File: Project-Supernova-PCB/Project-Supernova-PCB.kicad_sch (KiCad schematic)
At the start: 65 parts, among them J1 Conn_01x04, J10 Conn_01x02, J11 Screw_Terminal_01x02, J12 Screw_Terminal_01x02, J13 Conn_01x04, J14 Conn_01x04, J15 Conn_01x04, J2 Conn_01x04, J3 Conn_01x04, J4 Conn_Coaxial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

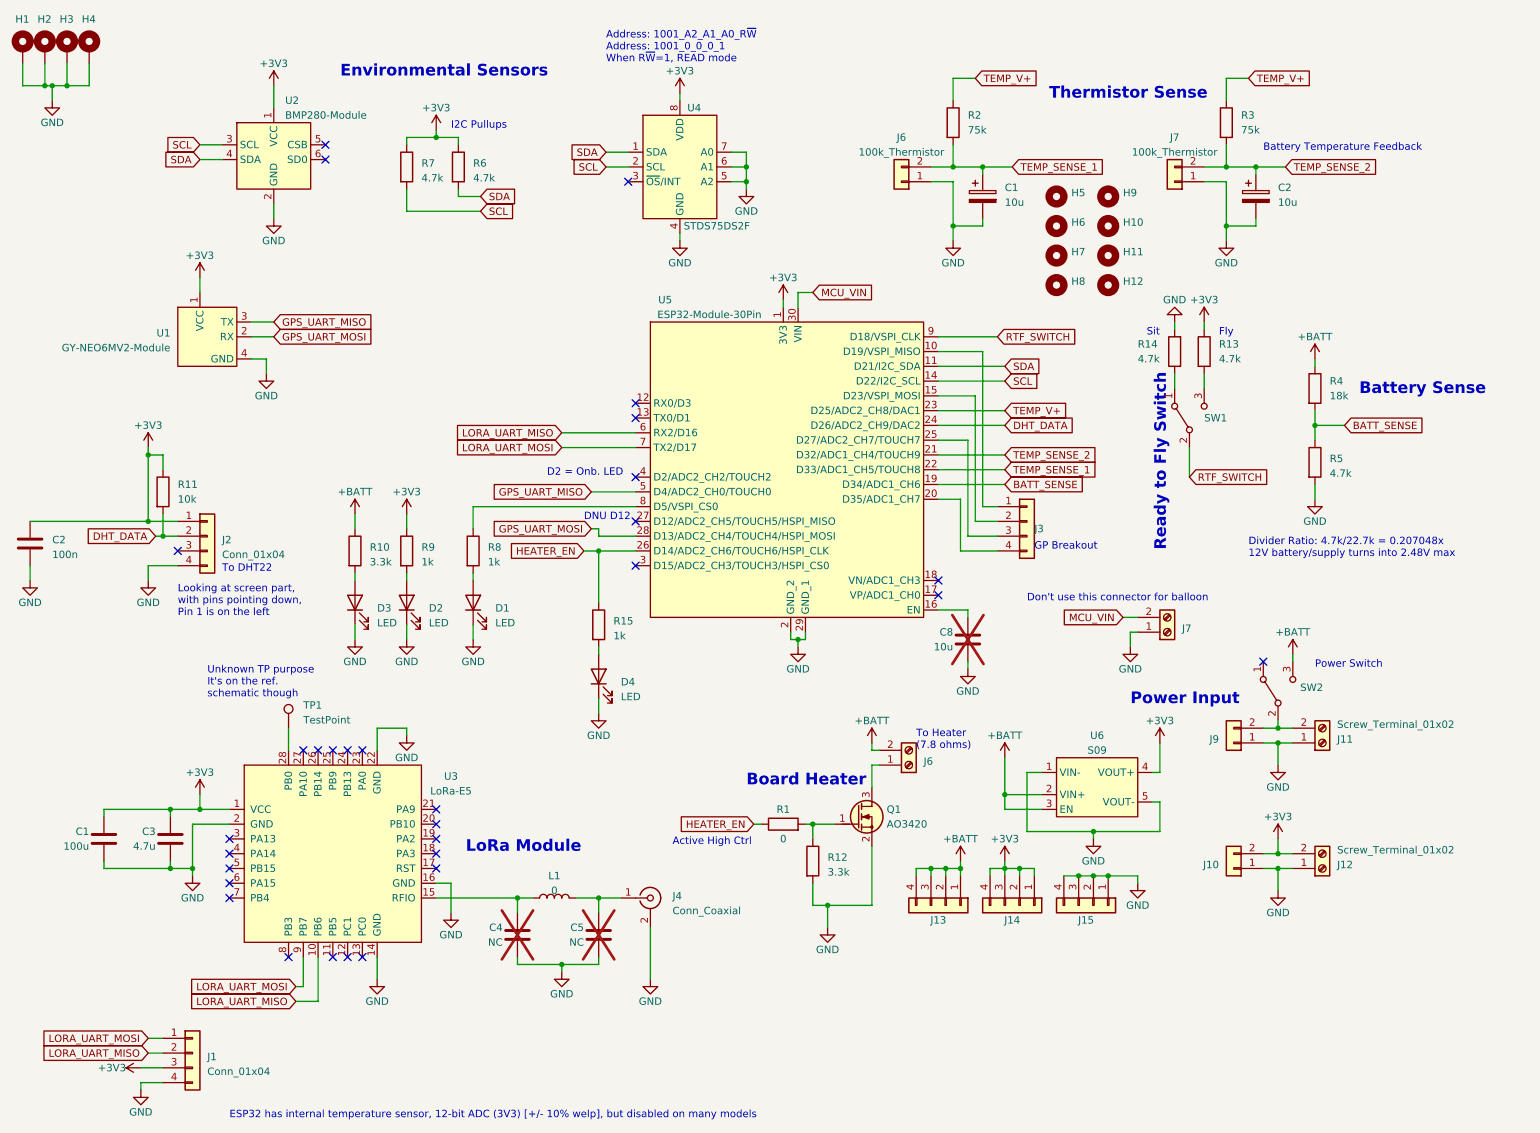
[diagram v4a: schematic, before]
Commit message: Clean up very messy schematic
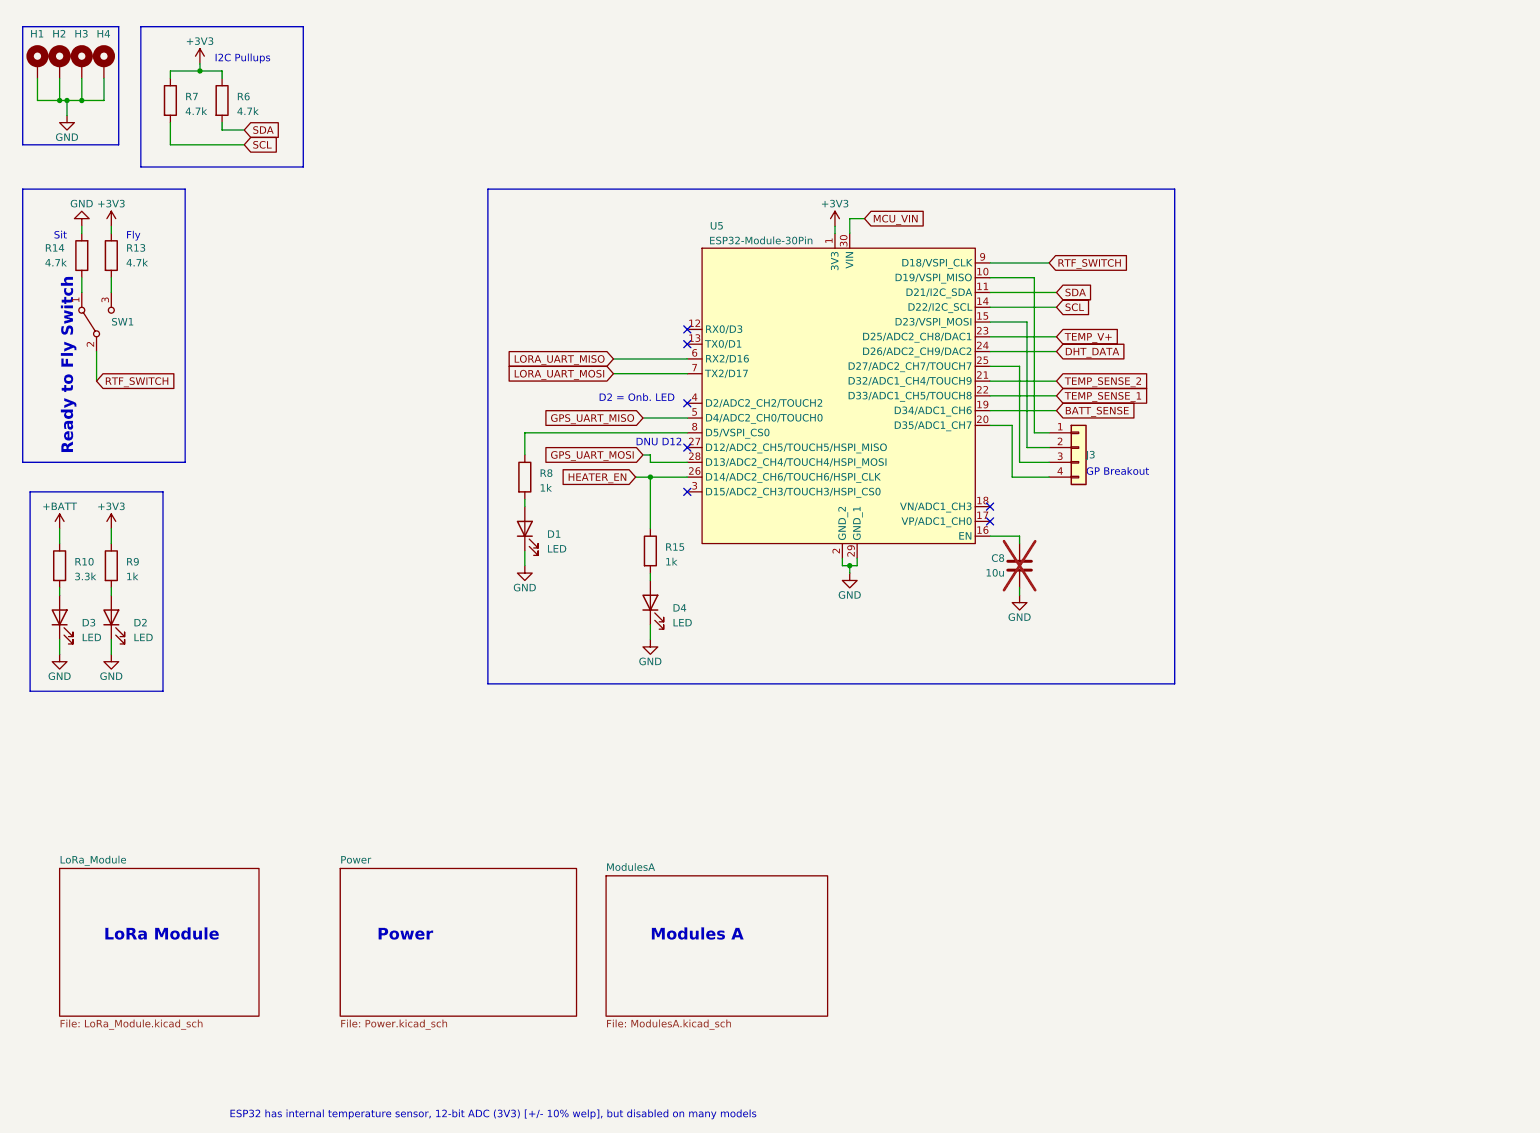
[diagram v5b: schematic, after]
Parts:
- removed C1, C2: 10u, Capacitor_SMD:C_1206_3216Metric_Pad1.33x1.80mm_HandSolder, symbol Device:C_Polarized
- removed C1: 100u, Capacitor_SMD:C_1206_3216Metric_Pad1.33x1.80mm_HandSolder, symbol Device:C
- removed C2: 100n, Capacitor_SMD:C_1206_3216Metric_Pad1.33x1.80mm_HandSolder, symbol Device:C
- removed C3: 4.7u, Capacitor_SMD:C_1206_3216Metric_Pad1.33x1.80mm_HandSolder, symbol Device:C
- removed C4, C5: NC, Capacitor_SMD:C_1206_3216Metric_Pad1.33x1.80mm_HandSolder, symbol Device:C
- removed H10, H11, H12, H5, H6, H7, H8, H9: MountingHole, MountingHole:MountingHole_2mm, symbol Mechanical:MountingHole
- removed J1, J13, J14, J15, J2: Conn_01x04, Connector_PinHeader_2.54mm:PinHeader_1x04_P2.54mm_Vertical, symbol Connector_Generic:Conn_01x04
- removed J10, J9: Conn_01x02, Connector_PinHeader_2.54mm:PinHeader_1x02_P2.54mm_Vertical, symbol Connector_Generic:Conn_01x02
- removed J11, J12, J6, J7: Screw_Terminal_01x02, TerminalBlock:TerminalBlock_bornier-2_P5.08mm, symbol Connector:Screw_Terminal_01x02
- removed J4: Conn_Coaxial, Connector_Coaxial:SMA_Wurth_60312002114503_Vertical, symbol Connector:Conn_Coaxial
- removed J6, J7: 100k_Thermistor, Connector_PinHeader_2.54mm:PinHeader_1x02_P2.54mm_Vertical, symbol Connector_Generic:Conn_01x02
- removed L1: 0, Inductor_SMD:L_1206_3216Metric_Pad1.42x1.75mm_HandSolder, symbol Device:L
- removed Q1: AO3420, Project-Supernova-Footprint-Lib:SOT-23-MassivePads-HandSolder, symbol PCM_Transistor_MOSFET_AKL:AO3420
- removed R1: 0, Resistor_SMD:R_1206_3216Metric_Pad1.30x1.75mm_HandSolder, symbol Device:R
- removed R11: 10k, Resistor_SMD:R_1206_3216Metric_Pad1.30x1.75mm_HandSolder, symbol Device:R
- removed R12: 3.3k, Resistor_SMD:R_1206_3216Metric_Pad1.30x1.75mm_HandSolder, symbol Device:R
- removed R2, R3: 75k, Resistor_SMD:R_1206_3216Metric_Pad1.30x1.75mm_HandSolder, symbol Device:R
- removed R4: 18k, Resistor_SMD:R_1206_3216Metric_Pad1.30x1.75mm_HandSolder, symbol Device:R
- removed R5: 4.7k, Resistor_SMD:R_1206_3216Metric_Pad1.30x1.75mm_HandSolder, symbol Device:R
- removed SW2: SW_SPDT, Button_Switch_THT:SW_Slide_1P2T_CK_OS102011MS2Q, symbol Switch:SW_SPDT
- removed TP1: TestPoint, TestPoint:TestPoint_Pad_D3.0mm, symbol Connector:TestPoint
- removed U1: GY-NEO6MV2-Module, Project-Supernova-Footprint-Lib:GY-NEO6MV2-Module, symbol Project-Supernova-Symbol-Lib:GY-NEO6MV2-Module
- removed U2: BMP280-Module, Project-Supernova-Footprint-Lib:BMP280-Module, symbol Project-Supernova-Symbol-Lib:BMP280-Module
- removed U3: LoRa-E5, Project-Supernova-Footprint-Lib:LoRa-E5_HandSolder, symbol Project-Supernova-Symbol-Lib:LoRa-E5
- removed U4: STDS75DS2F, Package_SO:MSOP-8_3x3mm_P0.65mm, symbol Project-Supernova-Symbol-Lib:STDS75DS2F
- removed U6: S09, Project-Supernova-Footprint-Lib:S09, symbol Project-Supernova-Symbol-Lib:S09_Buck_Boost
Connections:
- no-connect marks 31 -> 7
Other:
- added sheet LoRa_Module (LoRa_Module.kicad_sch)
- added sheet ModulesA (ModulesA.kicad_sch)
- added sheet Power (Power.kicad_sch)
- note added: "Modules A"
- note added: "Power"
- note removed: "Active High Ctrl"
- note removed: "Address: 1001_A2_A1_A0_R~{W} Address: 1001_0_0_0_1 When R~{W}=1, READ mode"
- note removed: "Battery Sense"
- note removed: "Battery Temperature Feedback"
- note removed: "Board Heater"
- note removed: "Divider Ratio: 4.7k/22.7k = 0.207048x 12V battery/supply turns into 2.48V max"
- note removed: "Don't use this connector for balloon"
- note removed: "Environmental Sensors"
- note removed: "Looking at screen part, with pins pointing down, Pin 1 is on the left"
- note removed: "Power Input"
- note removed: "Power Switch"
- note removed: "Thermistor Sense"
- note removed: "To DHT22"
- note removed: "To Heater (7.8 ohms)"
- note removed: "Unknown TP purpose It's on the ref. schematic though"
- moved on the sheet: C8, D1, D2, D3, D4, H1, H2, H3, H4, J3, R10, R13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
